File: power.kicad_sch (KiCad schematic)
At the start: 51 parts, among them CN8 POWER, U1 68000D, U10 74LS244, U11 74LS373, U12 74LS244, U13 74LS373, U2 FAT_AGNUS_8375, U32 74LS139, U34 74LS373, U35 74LS244, U36 74LS05, U37 74LS32, U5 GARY_5719, X1 XTAL

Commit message: DRAM chips replaced with SIMM module
Added logic to decode 2MB chip + 1.5MB slow
Rewired trapdoor slot
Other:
- title: Rämixx500 -> Rämixx500_max
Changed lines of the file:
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@@
 	(paper "A3")
 	(title_block
-		(title "Rämixx500")
-		(date "2020-04-04")
-		(rev "1")
+		(title "Rämixx500_max")
+		(date "2026-03-13")
+		(rev "2")
 		(company "SukkoPera")
 		(comment 1 "POWER AND DECOUPLING")

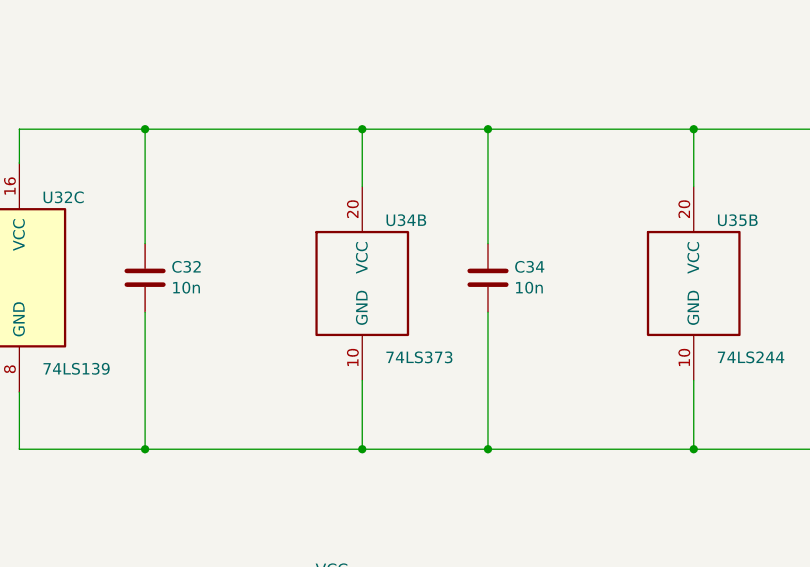
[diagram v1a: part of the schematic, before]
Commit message: optimized timing
removed CCK from RAM buffers to ease routing
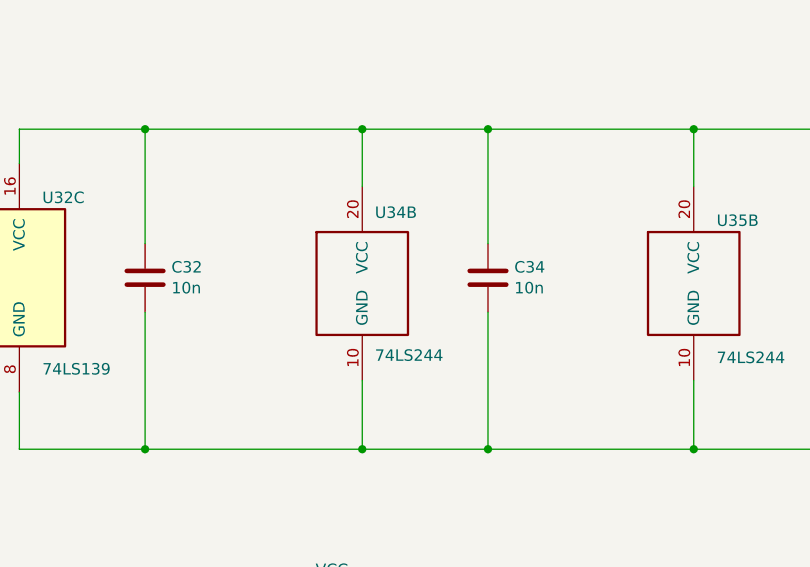
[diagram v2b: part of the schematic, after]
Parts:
- removed U34: 74LS373, Package_DIP:DIP-20_W7.62mm_Socket_LongPads, symbol 74ls373:74LS373
- added U34: 74LS244, symbol 74ls244:74LS244
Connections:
- net GND: now also U34.10 (GND)
- net VCC: now also U34.20 (VCC)
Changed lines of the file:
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@@
-	)
-	(symbol
-		(lib_id "74ls373:74LS373")
-		(at 97.028 180.594 0)
-		(unit 2)
-		(exclude_from_sim no)
-		(in_bom yes)
-		(on_board yes)
-		(dnp no)
-		(property "Reference" "U34"
-			(at 99.568 172.974 0)
-			(effects
-				(font
-					(size 1.27 1.27)
-				)
-				(justify left)
-			)
-		)
-		(property "Value" "74LS373"
-			(at 99.568 188.214 0)
-			(effects
-				(font
-					(size 1.27 1.27)
-				)
-				(justify left)
-			)
-		)
-		(property "Footprint" "Package_DIP:DIP-20_W7.62mm_Socket_LongPads"
-			(at 97.028 180.594 0)
-			(effects
-				(font
-					(size 1.27 1.27)
-				)
-				(hide yes)
-			)
-		)
-		(property "Datasheet" "http://www.ti.com/lit/gpn/sn74LS373"
-			(at 97.028 180.594 0)
-			(effects
-				(font
-					(size 1.27 1.27)
-				)
-				(hide yes)
-			)
-		)
-		(property "Description" ""
-			(at 97.028 180.594 0)
-			(effects
-				(font
-					(size 1.27 1.27)
-				)
-			)
-		)
-		(property "Section" "MEMORY"
-			(at 97.028 180.594 0)
-			(effects
-				(font
-					(size 1.27 1.27)
-				)
-				(hide yes)
-			)
-		)
-		(property "Cost" "0.68"
-			(at 97.028 180.594 0)
-			(effects
-				(font
-					(size 1.27 1.27)
-				)
-				(hide yes)
-			)
-		)
-		(property "MFG Name" "TI"
-			(at 97.028 180.594 0)
-			(effects
-				(font
-					(size 1.27 1.27)
-				)
-				(hide yes)
-			)
-		)
-		(property "MFG Part Num" "SN74LS373N"
-			(at 97.028 180.594 0)
-			(effects
-				(font
-					(size 1.27 1.27)
-				)
-				(hide yes)
-			)
-		)
-		(property "Required" "Y"
-			(at 97.028 180.594 0)
-			(effects
-				(font
-					(size 1.27 1.27)
-				)
-				(hide yes)
-			)
-		)
-		(pin "3"
-		)
-		(pin "7"
-		)
-		(pin "4"
-		)
-		(pin "2"
-		)
-		(pin "6"
-		)
-		(pin "10"
-		)
-		(pin "8"
-		)
-		(pin "12"
-		)
-		(pin "20"
-		)
-		(pin "18"
-		)
-		(pin "5"
-		)
-		(pin "17"
-		)
-		(pin "11"
-		)
-		(pin "14"
-		)
-		(pin "1"
-		)
-		(pin "9"
-		)
-		(pin "15"
-		)
-		(pin "13"
-		)
-		(pin "16"
-		)
-		(pin "19"
-		)
-		(instances
-			(project "Raemixx500"
-				(path "/a9c87613-fb8b-4be0-8e87-0d76f8b56421/00000000-0000-0000-0000-00005e9e4c57"
-					(reference "U34")
-					(unit 2)
-				)
-			)
-		)
 	)
 	(symbol
@@
 				)
 			)
+		)
+	)
+	(symbol
+		(lib_id "74ls244:74LS244")
+		(at 97.028 179.324 0)
+		(unit 2)
+		(exclude_from_sim no)
+		(in_bom yes)
+		(on_board yes)
+		(dnp no)
+		(property "Reference" "U34"
+			(at 98.425 172.085 0)
+			(effects
+				(font
+					(size 1.27 1.27)
+				)
+				(justify left)
+			)
+		)
+		(property "Value" "74LS244"
+			(at 98.425 187.96 0)
+			(effects
+				(font
+					(size 1.27 1.27)
+				)
+				(justify left)
+			)
+		)
+		(property "Footprint" ""
+			(at 97.028 179.324 0)
+			(effects
+				(font
+					(size 1.27 1.27)
+				)
+				(hide yes)
+			)
+		)
+		(property "Datasheet" "http://www.ti.com/lit/gpn/sn74LS244"
+			(at 97.028 179.324 0)
+			(effects
+				(font
+					(size 1.27 1.27)
+				)
+				(hide yes)
+			)
+		)
+		(property "Description" "8-bit Bus Buffer 3-State outputs"
+			(at 97.028 179.324 0)
+			(effects
+				(font
+					(size 1.27 1.27)
+				)
+				(hide yes)
+			)
+		)
+		(pin "4"
+		)
+		(pin "17"
+		)
+		(pin "5"
+		)
+		(pin "20"
+		)
+		(pin "13"
+		)
+		(pin "2"
+		)
+		(pin "18"
+		)
+		(pin "6"
+		)
+		(pin "12"
+		)
+		(pin "7"
+		)
+		(pin "8"
+		)
+		(pin "14"
+		)
+		(pin "11"
+		)
+		(pin "15"
+		)
+		(pin "19"
+		)
+		(pin "16"
+		)
+		(pin "1"
+		)
+		(pin "9"
+		)
+		(pin "3"
+		)
+		(pin "10"
+		)
+		(instances
+			(project "Raemixx500"
+				(path "/a9c87613-fb8b-4be0-8e87-0d76f8b56421/00000000-0000-0000-0000-00005e9e4c57"
+					(reference "U34")
+					(unit 2)
+				)
+			)

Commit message: removed JP2
some more small fixes
schematic is now more or less done I think
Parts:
- U34: footprint (none) -> Package_DIP:DIP-20_W7.62mm_Socket_LongPads
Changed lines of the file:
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@@
 			)
 		)
-		(property "Footprint" ""
+		(property "Footprint" "Package_DIP:DIP-20_W7.62mm_Socket_LongPads"
 			(at 97.028 179.324 0)
 			(effects

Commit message: - some IC are not socketed anymore to fit under shield
- updated logo
- silkscreen cleanup
- added pin1 indicator to solder jumpers
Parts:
- U32: footprint Package_DIP:DIP-16_W7.62mm_Socket_LongPads -> Package_DIP:DIP-16_W7.62mm_LongPads
- U34, U35: footprint Package_DIP:DIP-20_W7.62mm_Socket_LongPads -> Package_DIP:DIP-20_W7.62mm_LongPads
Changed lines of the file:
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@@
 			)
 		)
-		(property "Footprint" "Package_DIP:DIP-16_W7.62mm_Socket_LongPads"
+		(property "Footprint" "Package_DIP:DIP-16_W7.62mm_LongPads"
 			(at 58.928 179.324 0)
 			(effects
@@
 			)
 		)
-		(property "Footprint" "Package_DIP:DIP-20_W7.62mm_Socket_LongPads"
+		(property "Footprint" "Package_DIP:DIP-20_W7.62mm_LongPads"
 			(at 133.858 179.324 0)
 			(effects
@@
 			)
 		)
-		(property "Footprint" "Package_DIP:DIP-20_W7.62mm_Socket_LongPads"
+		(property "Footprint" "Package_DIP:DIP-20_W7.62mm_LongPads"
 			(at 97.028 179.324 0)
 			(effects

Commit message: Started cleaning up BOM
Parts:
- MT1, MT2, MT4, MT5, MT6, MT7: now left out of the parts list
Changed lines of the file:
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@@
 		(unit 1)
 		(exclude_from_sim no)
-		(in_bom yes)
+		(in_bom no)
 		(on_board yes)
 		(dnp no)
@@
 		(unit 1)
 		(exclude_from_sim no)
-		(in_bom yes)
+		(in_bom no)
 		(on_board yes)
 		(dnp no)
@@
 		(unit 1)
 		(exclude_from_sim no)
-		(in_bom yes)
+		(in_bom no)
 		(on_board yes)
 		(dnp no)
@@
 		(unit 1)
 		(exclude_from_sim no)
-		(in_bom yes)
+		(in_bom no)
 		(on_board yes)
 		(dnp no)
@@
 		(unit 1)
 		(exclude_from_sim no)
-		(in_bom yes)
+		(in_bom no)
 		(on_board yes)
 		(dnp no)
@@
 		(unit 1)
 		(exclude_from_sim no)
-		(in_bom yes)
-		(on_board yes)
-		(dnp no)
+		(in_bom no)
+		(on_board yes)
+		(dnp no)
